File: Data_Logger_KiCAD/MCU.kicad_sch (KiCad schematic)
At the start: 46 parts, among them J1 USB_C_Receptacle_USB2.0_16P, J2 Screw_Terminal_01x02, Q1 Q_NMOS_GSD, SW1 SW_Push, SW2 SW_Push, U2 ESP32-S3, Y2 Crystal, Y3 Crystal_GND24

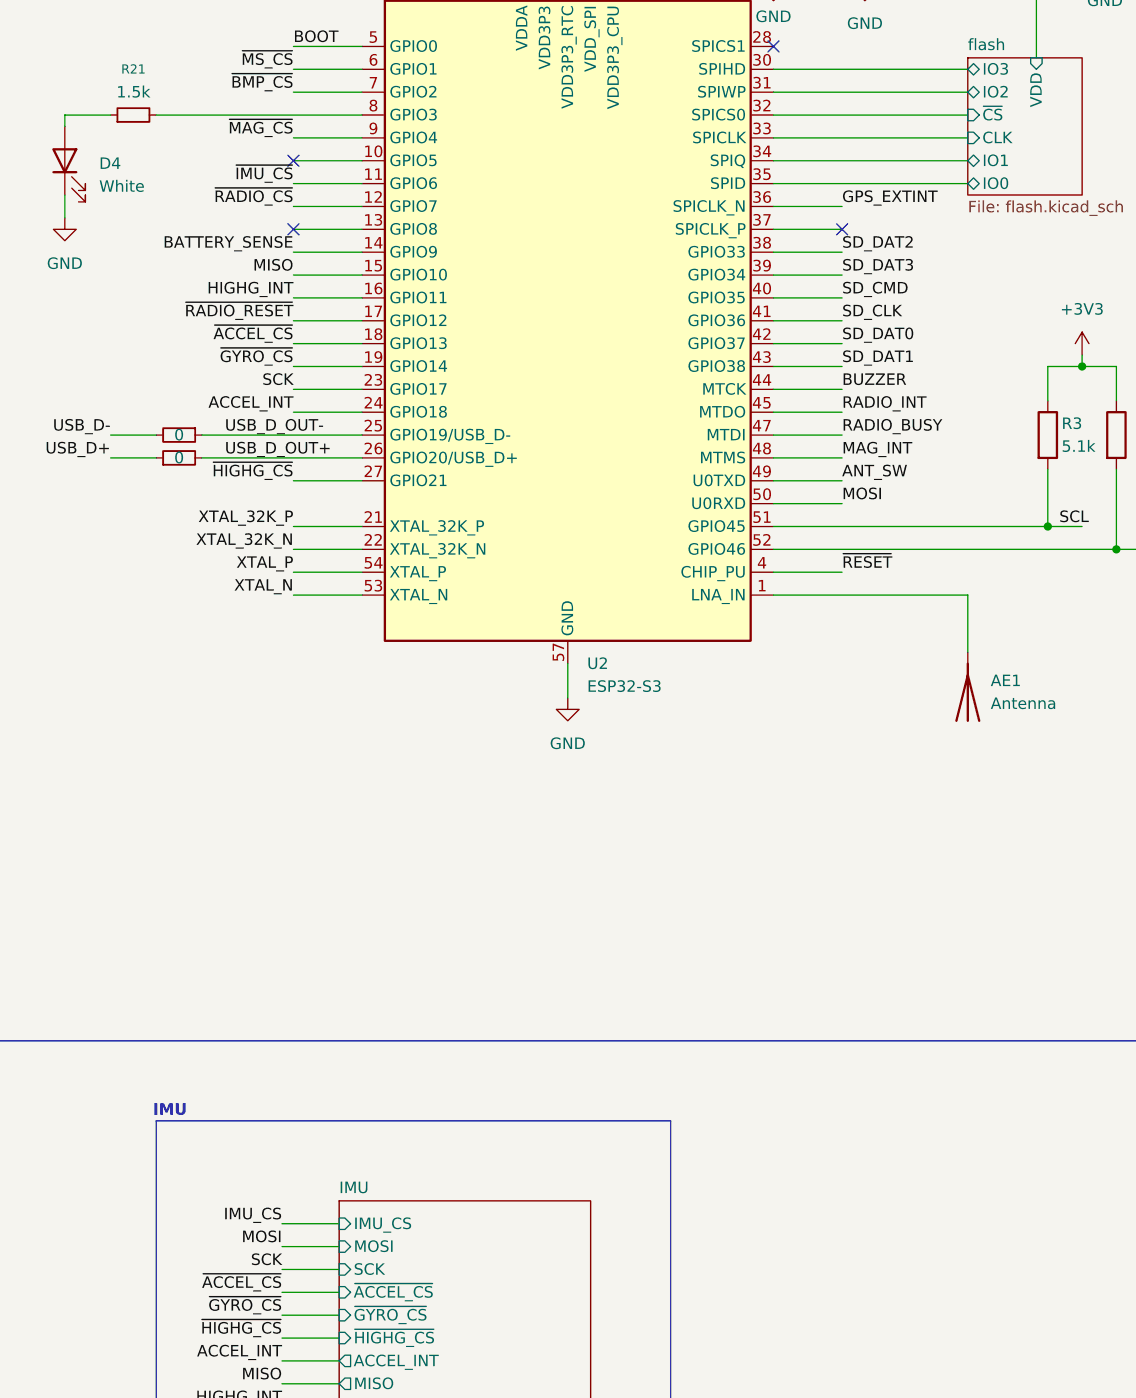
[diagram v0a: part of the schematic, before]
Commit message: layout power plane
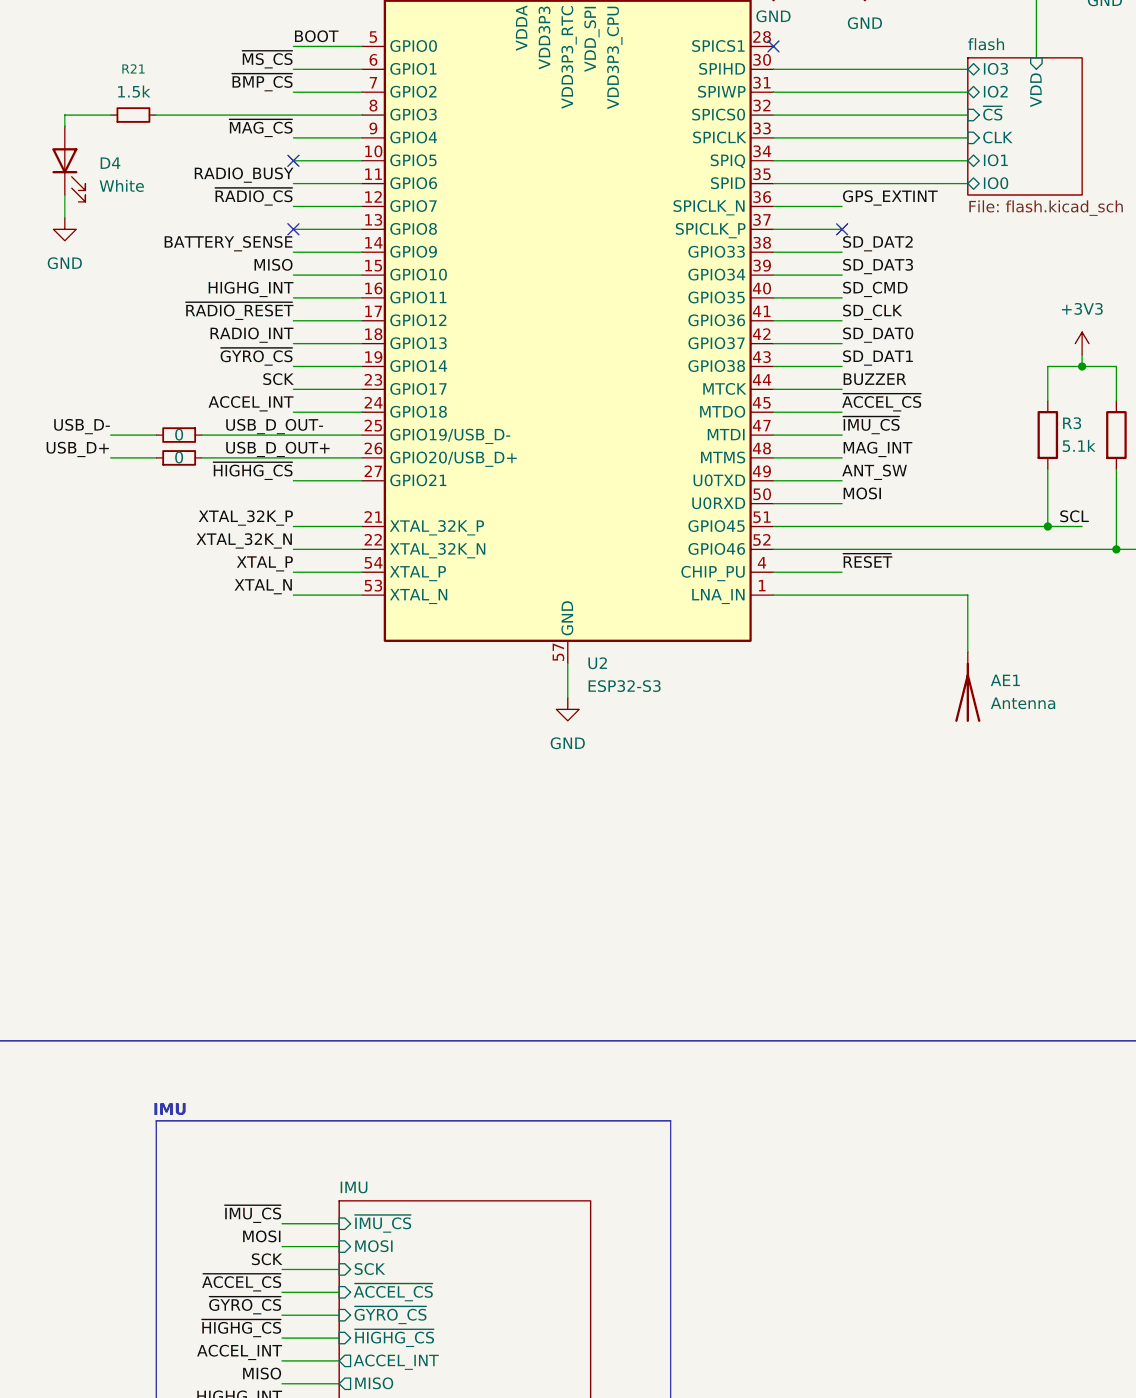
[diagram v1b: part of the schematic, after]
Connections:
- net RADIO_BUSY: now also U2.11 (GPIO6); no longer U2.47 (MTDI)
- net RADIO_INT: now also U2.18 (GPIO13); no longer U2.45 (MTDO)
- net ~{ACCEL_CS}: now also U2.45 (MTDO); no longer U2.18 (GPIO13)
- net ~{IMU_CS}: now also U2.47 (MTDI); no longer U2.11 (GPIO6)
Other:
- sheet IMU ports: added ~{IMU_CS}; removed IMU_CS
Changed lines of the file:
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@@
 		)
 	)
-	(label "RADIO_INT"
+	(label "~{ACCEL_CS}"
 		(at 193.04 133.35 0)
 		(effects
@@
 		)
 	)
-	(label "~{IMU_CS}"
+	(label "RADIO_BUSY"
 		(at 132.08 107.95 180)
 		(effects
@@
 		)
 	)
-	(label "IMU_CS"
+	(label "~{IMU_CS}"
 		(at 130.81 223.52 180)
 		(effects
@@
 		)
 	)
-	(label "RADIO_BUSY"
+	(label "~{IMU_CS}"
 		(at 193.04 135.89 0)
 		(effects
@@
 		)
 	)
-	(label "~{ACCEL_CS}"
+	(label "RADIO_INT"
 		(at 132.08 125.73 180)
 		(effects
@@
 			)
 		)
-		(pin "IMU_CS" input
+		(pin "~{IMU_CS}" input
 			(at 137.16 223.52 180)
 			(effects

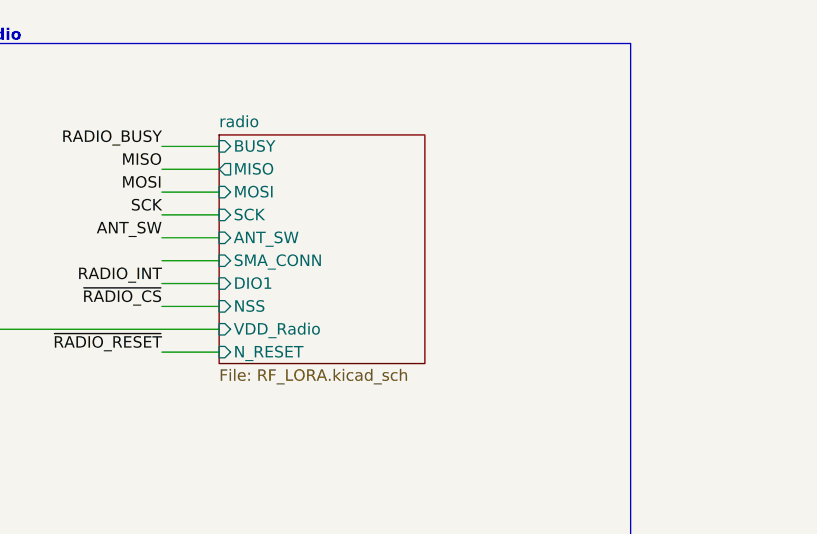
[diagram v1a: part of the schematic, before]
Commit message: Updates to board routing
Added SMA connector for radio, added additional SPI routing. Reworked some routing for other modules.
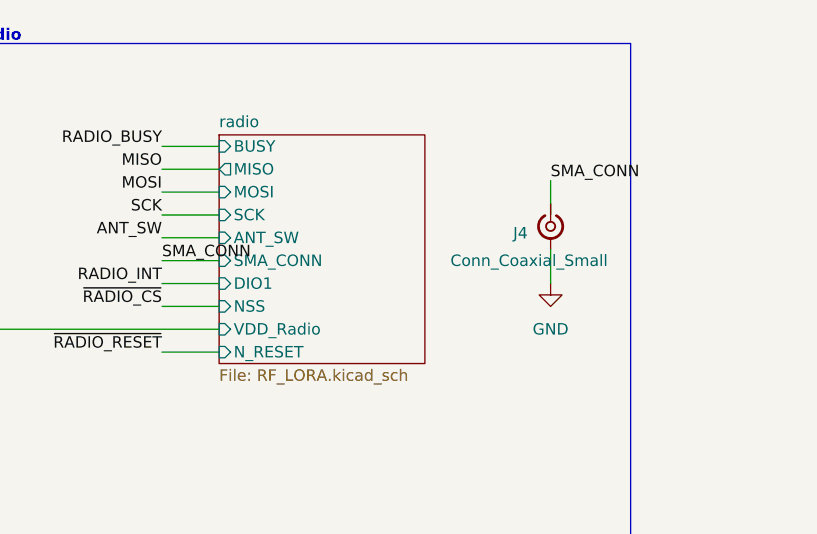
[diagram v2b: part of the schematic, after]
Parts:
- added J4: Conn_Coaxial_Small, Connector_Coaxial:SMA_Samtec_SMA-J-P-H-ST-EM1_EdgeMount, symbol Connector:Conn_Coaxial_Small
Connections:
- net GND: now also J4.2 (Ext)
- new net SMA_CONN: J4.1 (In)
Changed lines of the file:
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@@
 	(wire
 		(pts
+			(xy 312.42 71.12) (xy 312.42 68.58)
+		)
+		(stroke
+			(width 0)
+			(type default)
+		)
+	)
+	(wire
+		(pts
 			(xy 53.34 135.89) (xy 53.34 139.7)
 		)
@@
 	(wire
 		(pts
+			(xy 312.42 80.01) (xy 312.42 76.2)
+		)
+		(stroke
+			(width 0)
+			(type default)
+		)
+	)
+	(wire
+		(pts
 			(xy 132.08 128.27) (xy 139.7 128.27)
 		)
@@
 		)
 	)
+	(label "SMA_CONN"
+		(at 312.42 68.58 0)
+		(effects
+			(font
+				(size 1.27 1.27)
+			)
+			(justify left bottom)
+		)
+	)
+	(label "SMA_CONN"
+		(at 269.24 77.47 0)
+		(effects
+			(font
+				(size 1.27 1.27)
+			)
+			(justify left bottom)
+		)
+	)
 	(label "MAG_INT"
 		(at 379.73 127 180)
@@
 	(symbol
 		(lib_id "power:GND")
+		(at 312.42 80.01 0)
+		(unit 1)
+		(exclude_from_sim no)
+		(in_bom yes)
+		(on_board yes)
+		(dnp no)
+		(fields_autoplaced yes)
+		(property "Reference" "#PWR048"
+			(at 312.42 86.36 0)
+			(effects
+				(font
+					(size 1.27 1.27)
+				)
+				(hide yes)
+			)
+		)
+		(property "Value" "GND"
+			(at 312.42 85.09 0)
+			(effects
+				(font
+					(size 1.27 1.27)
+				)
+			)
+		)
+		(property "Footprint" ""
+			(at 312.42 80.01 0)
+			(effects
+				(font
+					(size 1.27 1.27)
+				)
+				(hide yes)
+			)
+		)
+		(property "Datasheet" ""
+			(at 312.42 80.01 0)
+			(effects
+				(font
+					(size 1.27 1.27)
+				)
+				(hide yes)
+			)
+		)
+		(property "Description" "Power symbol creates a global label with name \"GND\" , ground"
+			(at 312.42 80.01 0)
+			(effects
+				(font
+					(size 1.27 1.27)
+				)
+				(hide yes)
+			)
+		)
+		(pin "1"
+		)
+		(instances
+			(project "Data_Logger_Board"
+				(path "/db968e42-3ace-4cc9-9096-9d8f48135c40/795ab2be-9db7-4254-b05c-ac2b60177344"
+					(reference "#PWR048")
+					(unit 1)
+				)
+			)
+		)
+	)
+	(symbol
+		(lib_id "power:GND")
 		(at 162.56 165.1 0)
 		(unit 1)
@@
 					(unit 1)
 				)
+			)
+		)
+	)
+	(symbol
+		(lib_id "Connector:Conn_Coaxial_Small")
+		(at 312.42 73.66 270)
+		(unit 1)
+		(exclude_from_sim no)
+		(in_bom yes)
+		(on_board yes)
+		(dnp no)
+		(property "Reference" "J4"
+			(at 309.88 74.4106 90)
+			(effects
+				(font
+					(size 1.27 1.27)
+				)
+				(justify right)
+			)
+		)
+		(property "Value" "Conn_Coaxial_Small"
+			(at 318.77 77.47 90)
+			(effects
+				(font
+					(size 1.27 1.27)
+				)
+				(justify right)
+			)
+		)
+		(property "Footprint" "Connector_Coaxial:SMA_Samtec_SMA-J-P-H-ST-EM1_EdgeMount"
+			(at 312.42 73.66 0)
+			(effects
+				(font
+					(size 1.27 1.27)
+				)
+				(hide yes)
+			)
+		)
+		(property "Datasheet" "~"
+			(at 312.42 73.66 0)
+			(effects
+				(font
+					(size 1.27 1.27)
+				)
+				(hide yes)
+			)
+		)
+		(property "Description" "small coaxial connector (BNC, SMA, SMB, SMC, Cinch/RCA, LEMO, ...)"
+			(at 312.42 73.66 0)
+			(effects
+				(font
+					(size 1.27 1.27)
+				)
+				(hide yes)
+			)
+		)
+		(pin "2"
+		)
+		(pin "1"
+		)
+		(instances
+			(project ""
+				(path "/db968e42-3ace-4cc9-9096-9d8f48135c40/795ab2be-9db7-4254-b05c-ac2b60177344"
+					(reference "J4")
+					(unit 1)
+				)

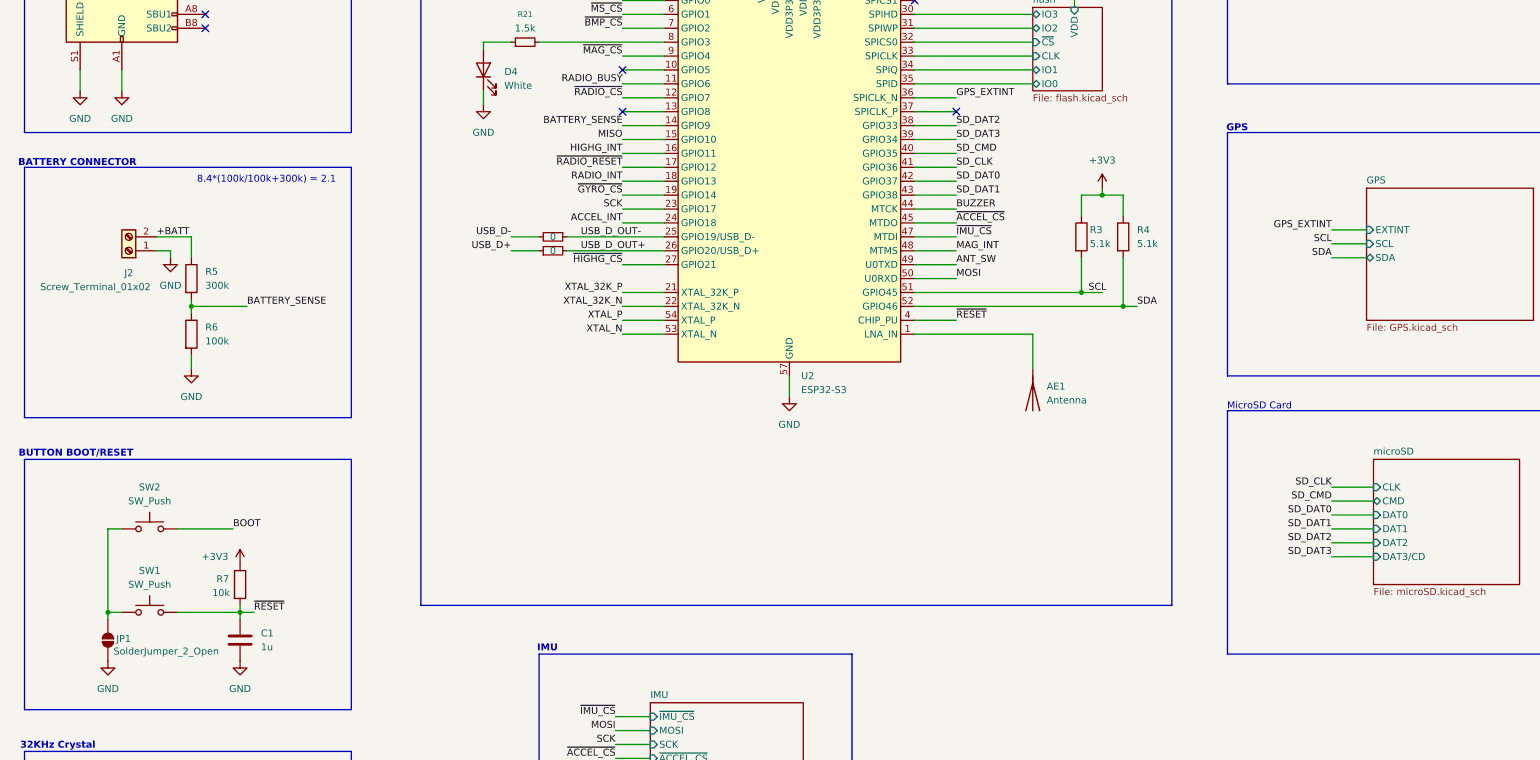
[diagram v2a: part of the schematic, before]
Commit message: layout
fix rf, usb netclass, add timepulse, round dimensions to even number, re-route GPS, 22 ohm in usb line, buttons to front, reg to front, change solder jumper for conn
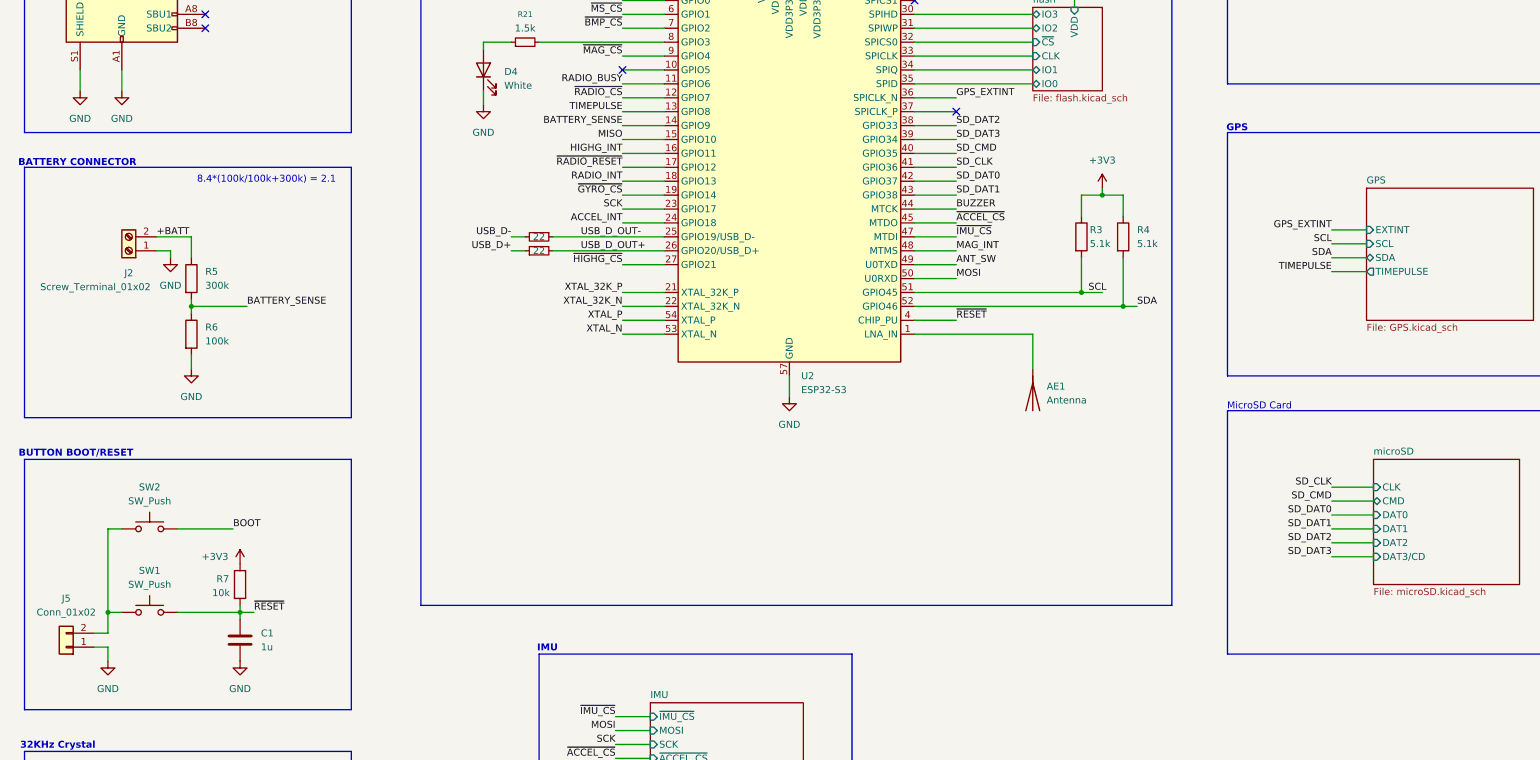
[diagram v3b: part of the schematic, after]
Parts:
- removed JP1: SolderJumper_2_Open, Jumper:SolderJumper-2_P1.3mm_Open_RoundedPad1.0x1.5mm, symbol Jumper:SolderJumper_2_Open
- added J5: Conn_01x02, Connector_PinHeader_1.27mm:PinHeader_1x02_P1.27mm_Vertical, symbol Connector_Generic:Conn_01x02
- R11, R12: value 0 -> 22; LCSC (none) -> C25092
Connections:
- net GND: now also J5.1 (Pin_1)
- net at SW1.1, SW2.1: now also J5.2 (Pin_2)
- net TIMEPULSE: now reaches U2.13 (GPIO8)
- no-connect marks 6 -> 5
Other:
- sheet GPS ports: added TIMEPULSE; removed none

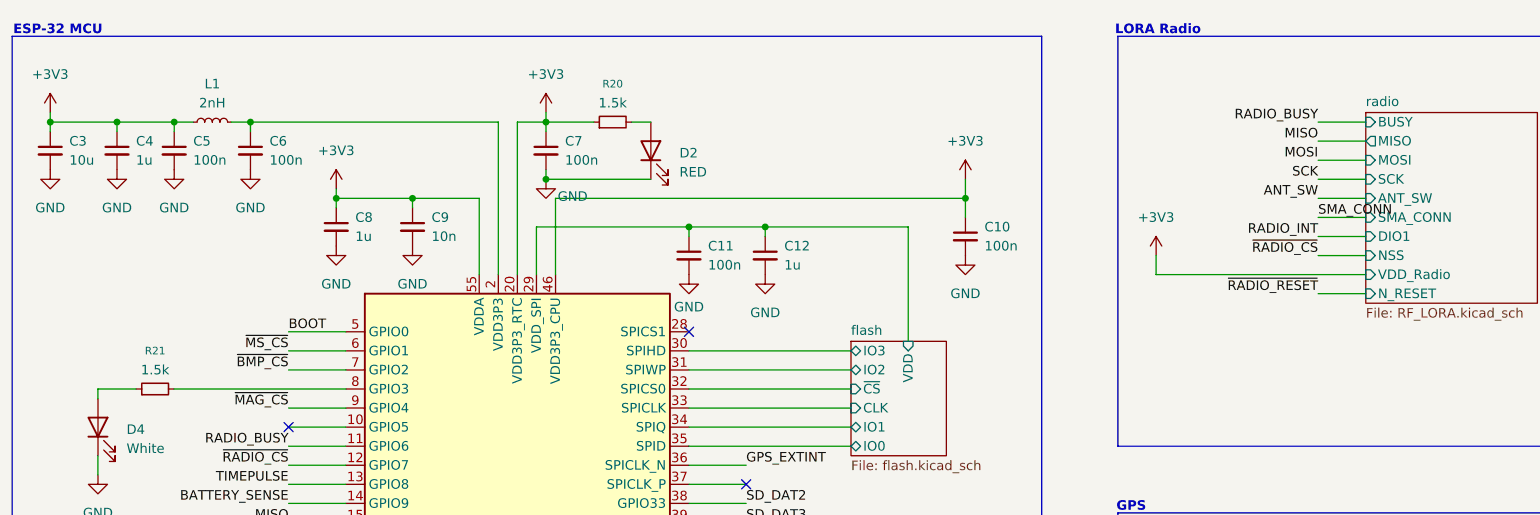
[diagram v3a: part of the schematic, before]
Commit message: review LCSC fields
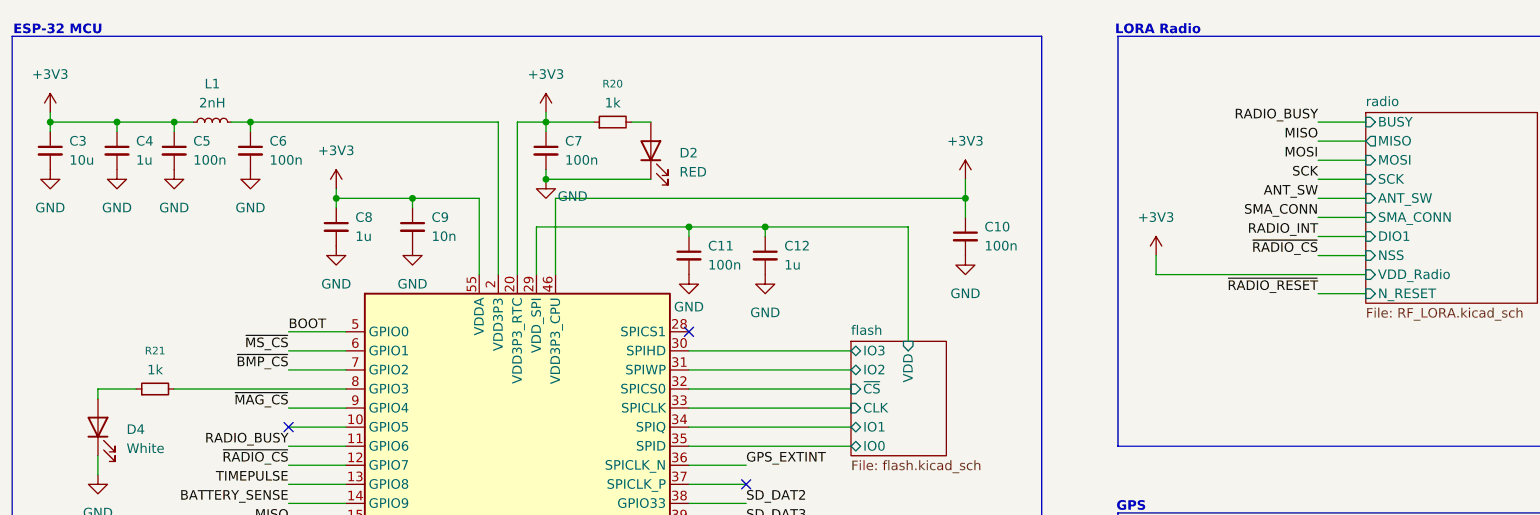
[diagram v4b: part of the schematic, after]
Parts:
- D2, D4: LCSC C2290 -> (none)
- R20, R21: value 1.5k -> 1k; LCSC C25867 -> C11702
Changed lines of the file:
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@@
 	)
 	(label "SMA_CONN"
-		(at 269.24 77.47 0)
+		(at 269.24 77.47 180)
 		(effects
 			(font
 				(size 1.27 1.27)
 			)
-			(justify left bottom)
+			(justify right bottom)
 		)
 	)
@@
 			)
 		)
-		(property "Value" "1.5k"
+		(property "Value" "1k"
 			(at 175.26 62.23 90)
 			(effects
@@
 			)
 		)
-		(property "LCSC" "C25867"
+		(property "LCSC" "C11702"
 			(at 175.26 64.77 90)
 			(effects
@@
 			)
 		)
-		(property "LCSC" "C2290"
+		(property "LCSC" ""
 			(at 106.68 105.41 90)
 			(effects
@@
 			)
 		)
-		(property "LCSC" "C2290"
+		(property "LCSC" ""
 			(at 180.34 68.58 90)
 			(effects
@@
 			)
 		)
-		(property "Value" "1.5k"
+		(property "Value" "1k"
 			(at 114.3 97.79 90)
 			(effects
@@
 			)
 		)
-		(property "LCSC" "C25867"
+		(property "LCSC" "C11702"
 			(at 114.3 100.33 90)
 			(effects
